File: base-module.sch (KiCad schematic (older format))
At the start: 0 parts

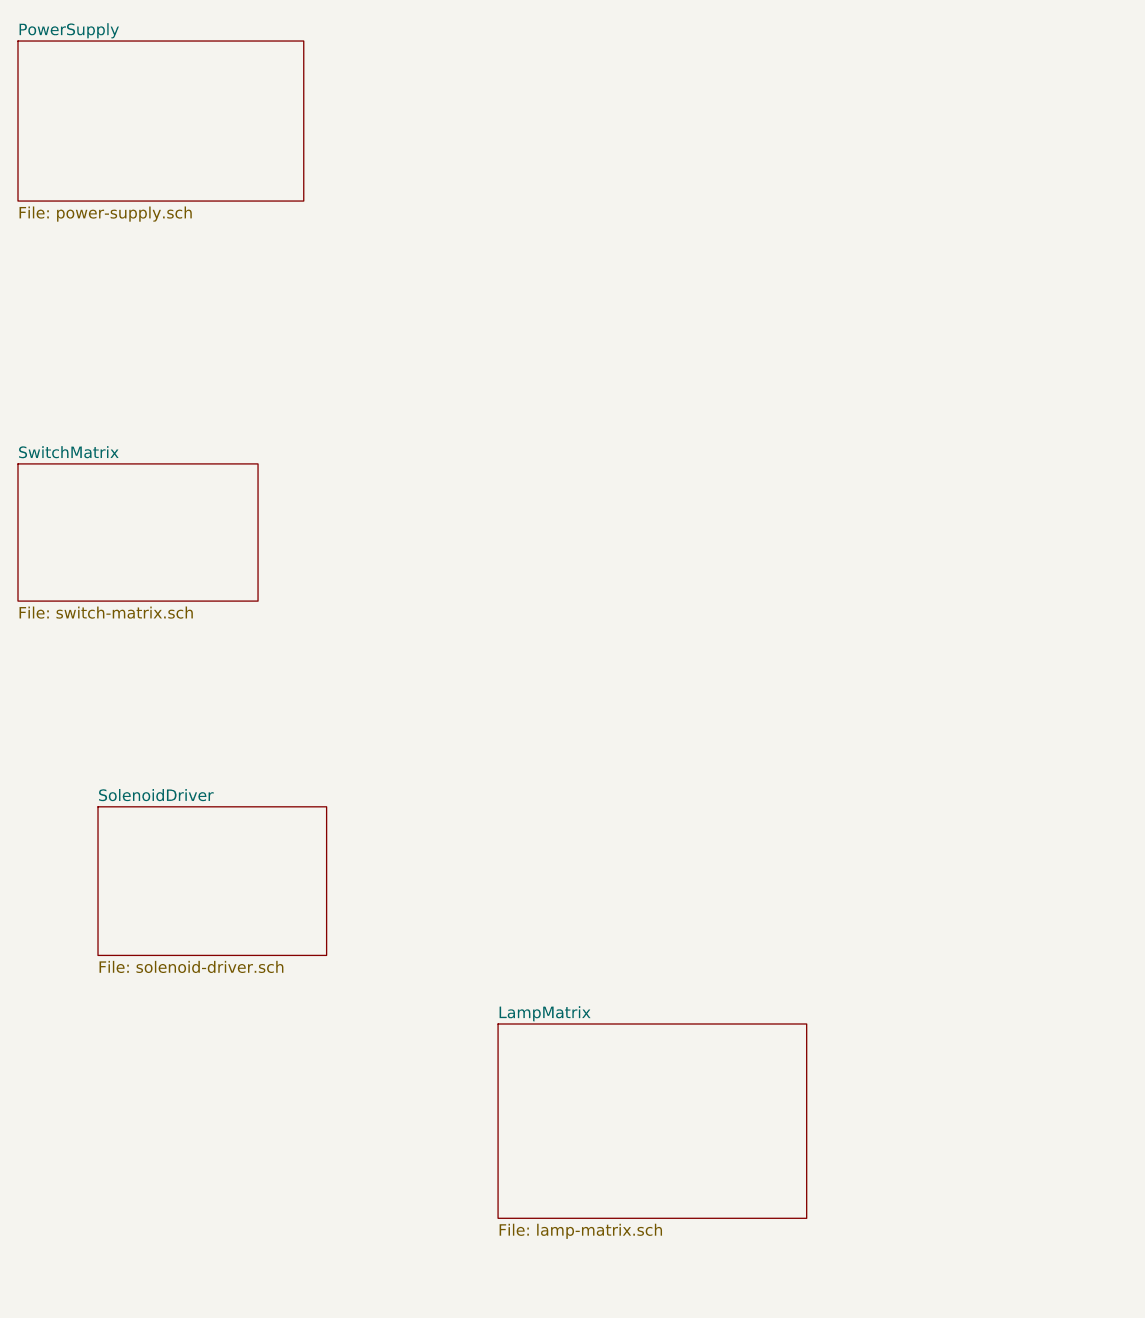
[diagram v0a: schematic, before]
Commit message: Adding hierarchy of schematics to project
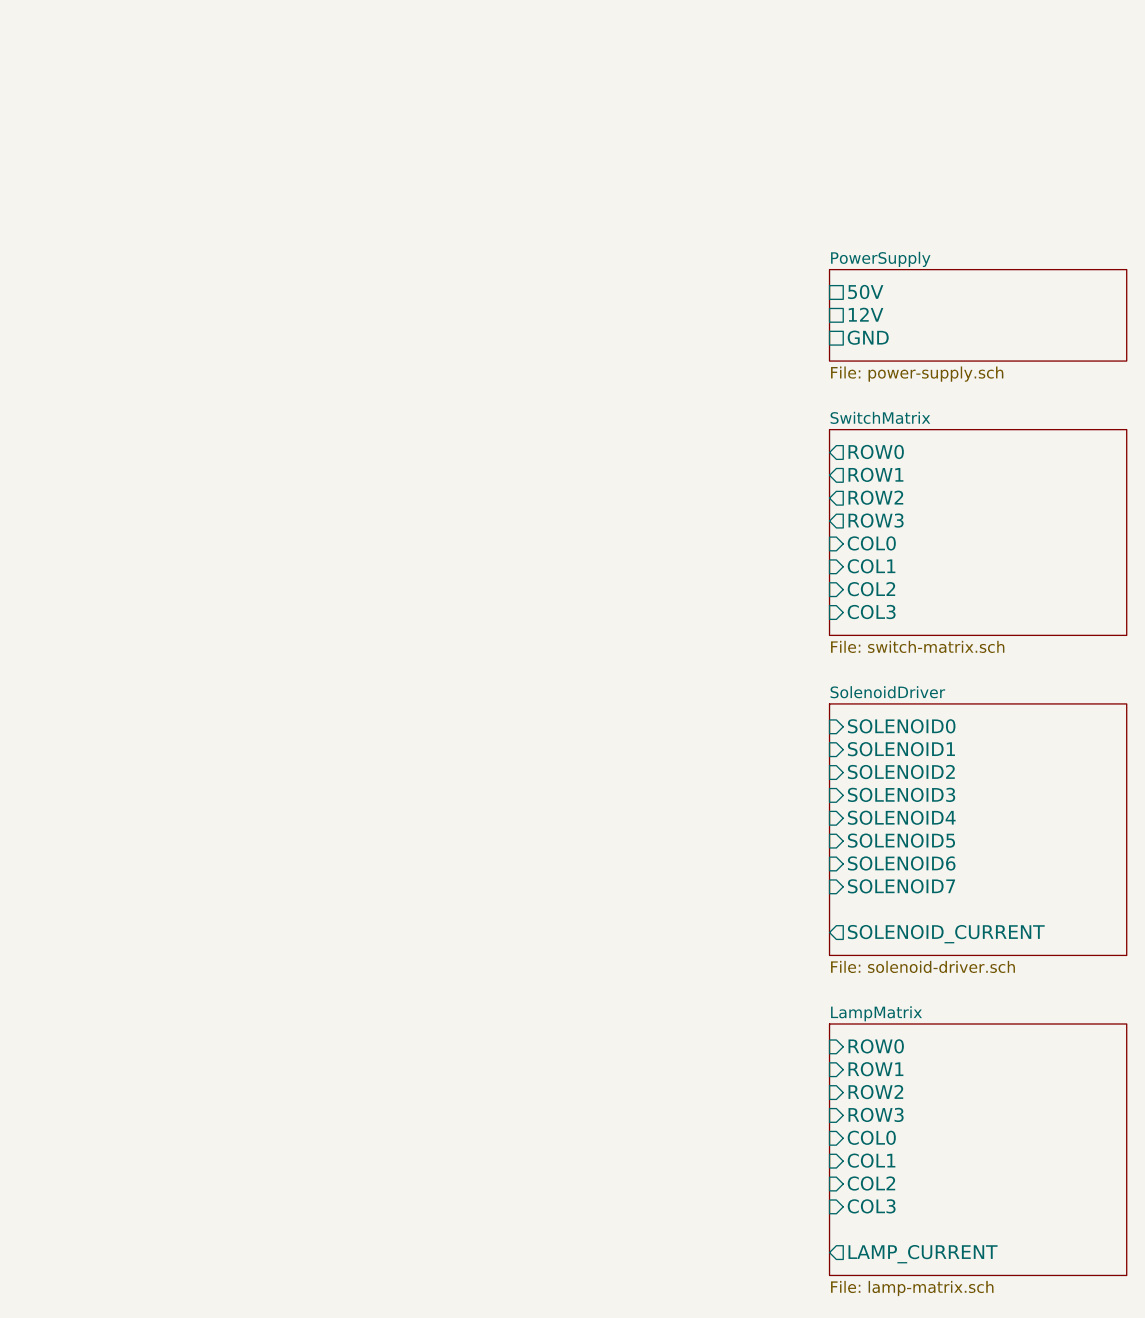
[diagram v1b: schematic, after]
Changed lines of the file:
@@
-EESchema Schematic File Version 2  date 4/8/2013 11:50:23 PM
+EESchema Schematic File Version 2  date 4/9/2013 12:24:46 AM
 LIBS:power
 LIBS:device
@@
 $Descr USLetter 11000 8500
 encoding utf-8
-Sheet 1 4
+Sheet 1 5
 Title ""
 Date "9 apr 2013"
@@
 $EndDescr
 $Sheet
-S 5250 3550 1050 600
+S 8800 3400 1300 900
 U 51638E9B
 F0 "SwitchMatrix" 50
 F1 "switch-matrix.sch" 50
+F2 "ROW0" O L 8800 3500 60
+F3 "ROW1" O L 8800 3600 60
+F4 "ROW2" O L 8800 3700 60
+F5 "ROW3" O L 8800 3800 60
+F6 "COL0" I L 8800 3900 60
+F7 "COL1" I L 8800 4000 60
+F8 "COL2" I L 8800 4100 60
+F9 "COL3" I L 8800 4200 60
 $EndSheet
 $Sheet
-S 7350 6000 1350 850
+S 8800 6000 1300 1100
 U 51638EC2
 F0 "LampMatrix" 50
 F1 "lamp-matrix.sch" 50
+F2 "ROW0" I L 8800 6100 60
+F3 "ROW1" I L 8800 6200 60
+F4 "ROW2" I L 8800 6300 60
+F5 "ROW3" I L 8800 6400 60
+F6 "COL0" I L 8800 6500 60
+F7 "COL1" I L 8800 6600 60
+F8 "COL2" I L 8800 6700 60
+F9 "COL3" I L 8800 6800 60
+F10 "LAMP_CURRENT" O L 8800 7000 60
 $EndSheet
 $Sheet
-S 5600 5050 1000 650
+S 8800 2700 1300 400
+U 51638FEE
+F0 "PowerSupply" 50
+F1 "power-supply.sch" 50
+F2 "50V" U L 8800 2800 60
+F3 "12V" U L 8800 2900 60
+F4 "GND" U L 8800 3000 60
+$EndSheet
+$Sheet
+S 8800 4600 1300 1100
 U 51638EDE
 F0 "SolenoidDriver" 50
 F1 "solenoid-driver.sch" 50
-$EndSheet
-$Sheet
-S 5250 1700 1250 700
-U 51638FEE
-F0 "PowerSupply" 50
-F1 "power-supply.sch" 50
+F2 "SOLENOID0" I L 8800 4700 60
+F3 "SOLENOID1" I L 8800 4800 60
+F4 "SOLENOID2" I L 8800 4900 60
+F5 "SOLENOID3" I L 8800 5000 60
+F6 "SOLENOID4" I L 8800 5100 60
+F7 "SOLENOID5" I L 8800 5200 60
+F8 "SOLENOID6" I L 8800 5300 60
+F9 "SOLENOID7" I L 8800 5400 60
+F10 "SOLENOID_CURRENT" O L 8800 5600 60
 $EndSheet
 $EndSCHEMATC
